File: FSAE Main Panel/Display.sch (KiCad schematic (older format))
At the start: 44 parts, among them U501 TLC6C598

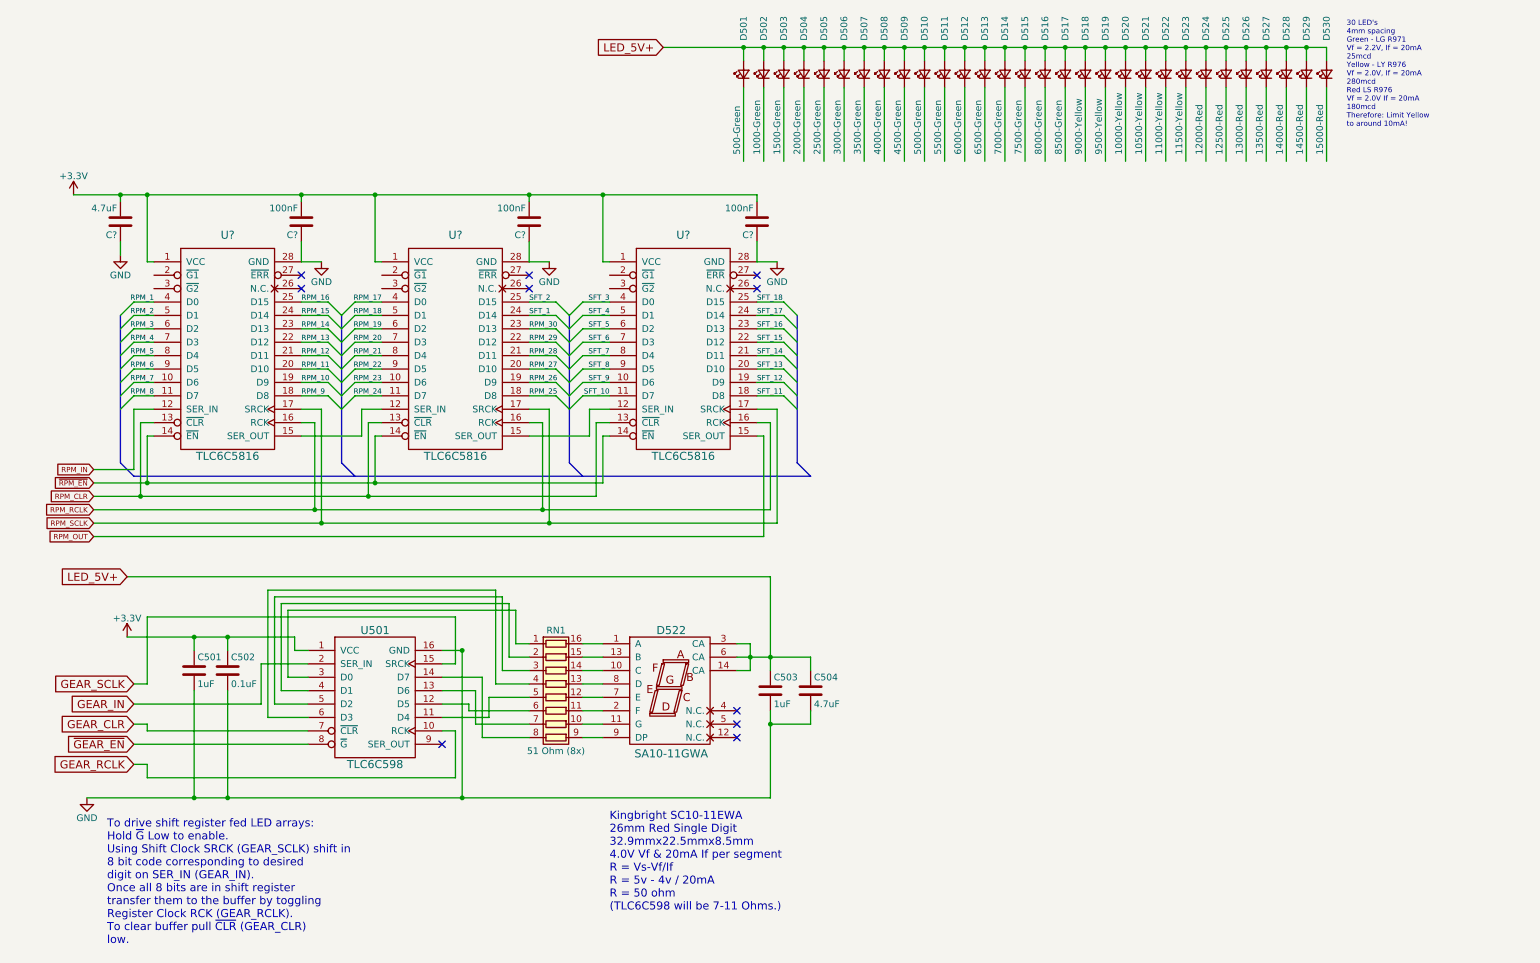
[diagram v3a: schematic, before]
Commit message: Added Blue shift LEDs and proper resistor arrays
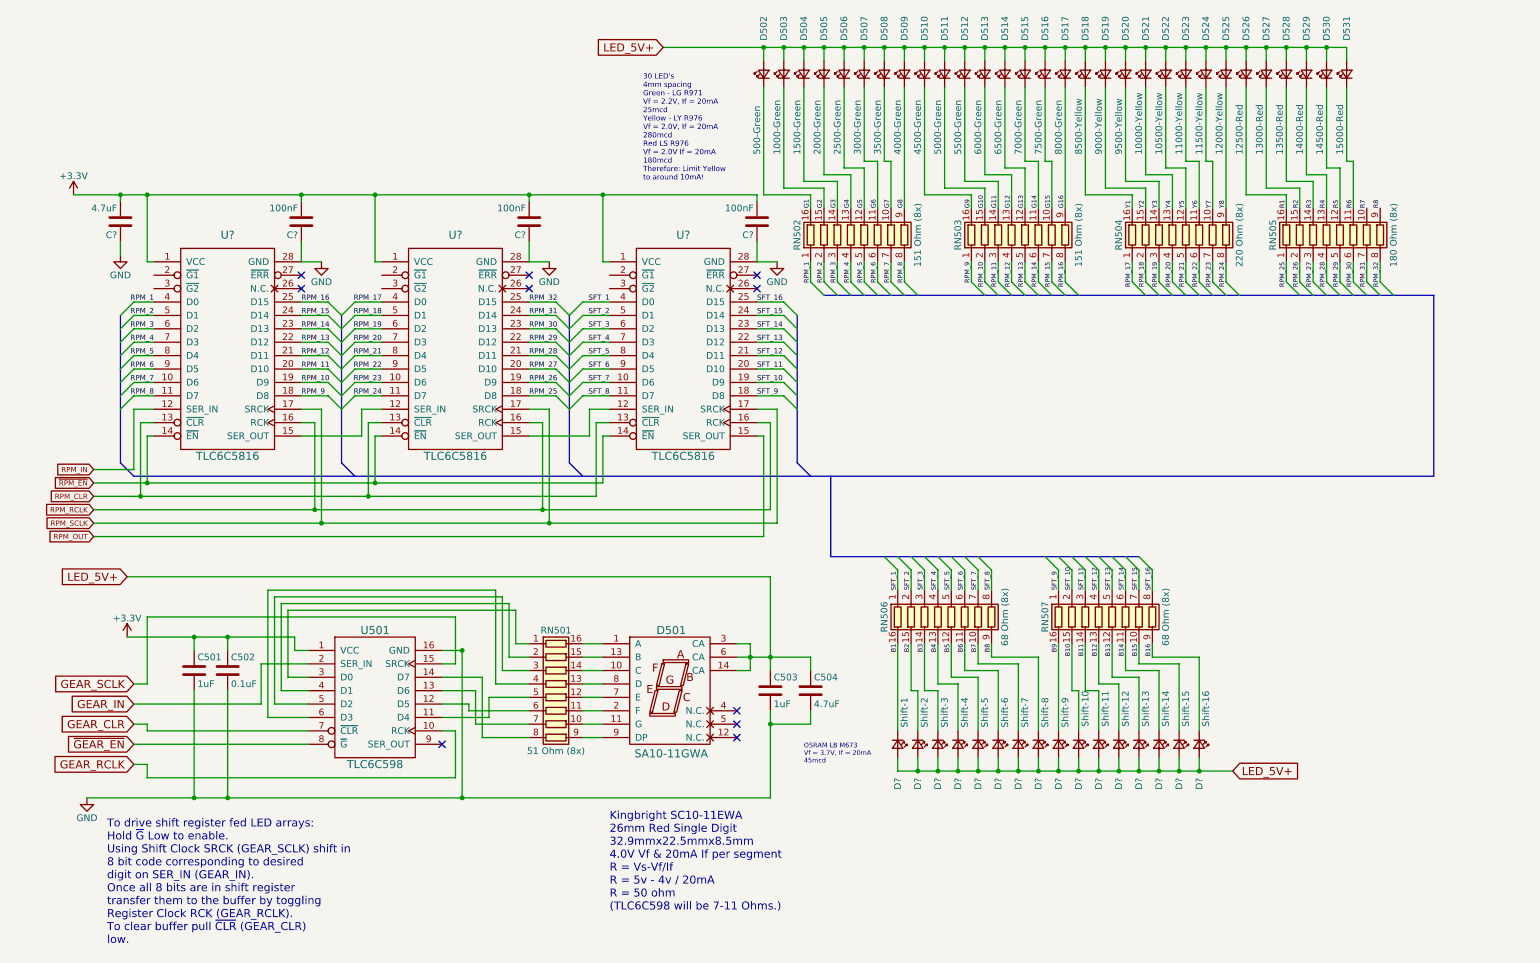
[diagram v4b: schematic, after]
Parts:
- removed D501: 500-Green, LEDs:LED_0805, symbol LED_Small
- added D531: 15000-Red, LEDs:LED_0805, symbol LED_Small
- added D?: Shift-1, LEDs:LED_0805, symbol LED_Small
- added D?: Shift-2, LEDs:LED_0805, symbol LED_Small
- added D?: Shift-3, LEDs:LED_0805, symbol LED_Small
- added D?: Shift-4, LEDs:LED_0805, symbol LED_Small
- added D?: Shift-5, LEDs:LED_0805, symbol LED_Small
- added D?: Shift-6, LEDs:LED_0805, symbol LED_Small
- added D?: Shift-7, LEDs:LED_0805, symbol LED_Small
- added D?: Shift-8, LEDs:LED_0805, symbol LED_Small
- added D?: Shift-9, LEDs:LED_0805, symbol LED_Small
- added D?: Shift-10, LEDs:LED_0805, symbol LED_Small
- added D?: Shift-11, LEDs:LED_0805, symbol LED_Small
- added D?: Shift-12, LEDs:LED_0805, symbol LED_Small
- added D?: Shift-13, LEDs:LED_0805, symbol LED_Small
- added D?: Shift-14, LEDs:LED_0805, symbol LED_Small
- added D?: Shift-15, LEDs:LED_0805, symbol LED_Small
- added D?: Shift-16, LEDs:LED_0805, symbol LED_Small
- added RN502, RN503: 151 Ohm (8x), Housings_SOIC:SOIC-16W_5.3x10.2mm_Pitch1.27mm, symbol R_Pack08
- added RN504: 220 Ohm (8x), Housings_SOIC:SOIC-16W_5.3x10.2mm_Pitch1.27mm, symbol R_Pack08
- added RN505: 180 Ohm (8x), Housings_SOIC:SOIC-16W_5.3x10.2mm_Pitch1.27mm, symbol R_Pack08
- added RN506, RN507: 68 Ohm (8x), Housings_SOIC:SOIC-16W_5.3x10.2mm_Pitch1.27mm, symbol R_Pack08
- D502: value 1000-Green -> 500-Green
- D503: value 1500-Green -> 1000-Green
- D504: value 2000-Green -> 1500-Green
- D505: value 2500-Green -> 2000-Green
- D506: value 3000-Green -> 2500-Green
- D507: value 3500-Green -> 3000-Green
- D508: value 4000-Green -> 3500-Green
- D509: value 4500-Green -> 4000-Green
- D510: value 5000-Green -> 4500-Green
- D511: value 5500-Green -> 5000-Green
- D512: value 6000-Green -> 5500-Green
- D513: value 6500-Green -> 6000-Green
- D514: value 7000-Green -> 6500-Green
- D515: value 7500-Green -> 7000-Green
- D516: value 8000-Green -> 7500-Green
- D517: value 8500-Green -> 8000-Green
- D518: value 9000-Yellow -> 8500-Yellow
- D519: value 9500-Yellow -> 9000-Yellow
- D520: value 10000-Yellow -> 9500-Yellow
- D521: value 10500-Yellow -> 10000-Yellow
- D522: value 11000-Yellow -> 10500-Yellow
- D523: value 11500-Yellow -> 11000-Yellow
- D524: value 12000-Red -> 11500-Yellow; Part Number LG R971 -> LY R976
- D525: value 12500-Red -> 12000-Yellow; Part Number LG R971 -> LY R976
- D526: value 13000-Red -> 12500-Red; Part Number LG R971 -> LS R976
- D527: value 13500-Red -> 13000-Red; Part Number LG R971 -> LS R976
- D528: value 14000-Red -> 13500-Red; Part Number LG R971 -> LS R976
- D529: value 14500-Red -> 14000-Red; Part Number LG R971 -> LS R976
- D530: value 15000-Red -> 14500-Red; Part Number LG R971 -> LS R976
- renumbered D522 to D501, RN1 to RN501
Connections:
- net labels added: B1, B10, B11, B12, B13, B14, B15, B16, B2, B3, B4, B5, B6, B7, B8, B9, G1, G10, G11, G12, G13, G14, G15, G16, G2, G3, G4, G5, G6, G7, G8, G9, R1, R2, R3, R4, R5, R6, R7, R8, RPM_31, RPM_32, Y1, Y2, Y3, Y4, Y5, Y6, Y7, Y8
- net labels removed: SFT_17, SFT_18
- wire segments 244 -> 407
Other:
- note added: "OSRAM LB M673\nVf = 3.7V, If = 20mA\n45mcd"

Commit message: Finished most LEDs, begun power regulators
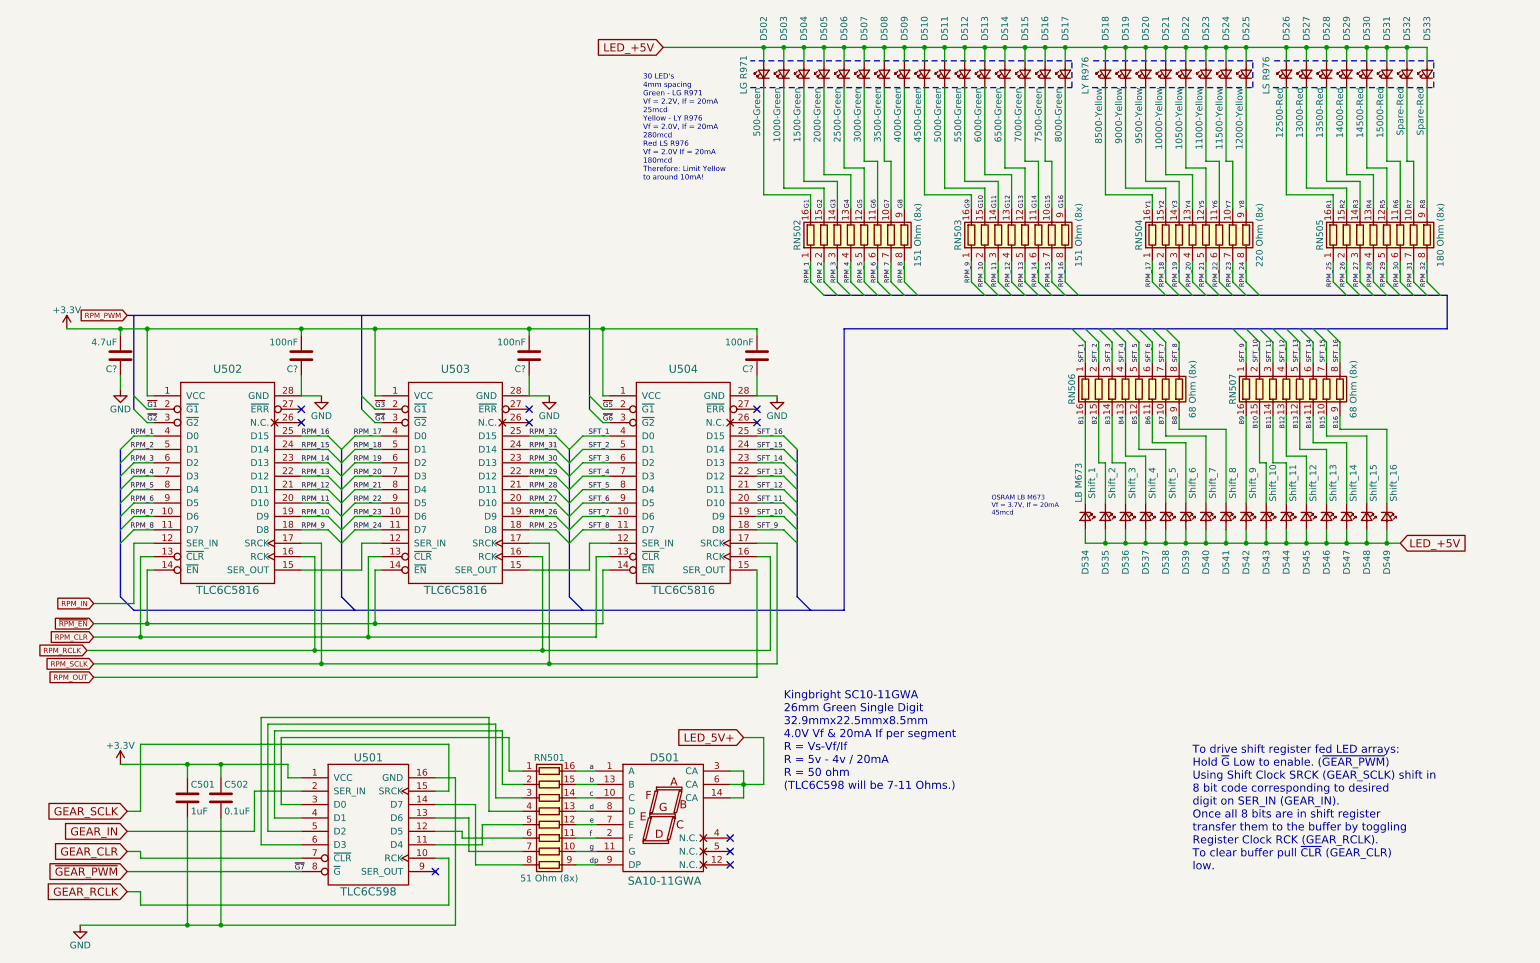
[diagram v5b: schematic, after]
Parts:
- removed C503: 1uF, symbol C
- removed C504: 4.7uF, symbol C
- removed D?: Shift-2, LEDs:LED_0805, symbol LED_Small
- removed D?: Shift-3, LEDs:LED_0805, symbol LED_Small
- removed D?: Shift-4, LEDs:LED_0805, symbol LED_Small
- removed D?: Shift-5, LEDs:LED_0805, symbol LED_Small
- removed D?: Shift-6, LEDs:LED_0805, symbol LED_Small
- removed D?: Shift-7, LEDs:LED_0805, symbol LED_Small
- removed D?: Shift-8, LEDs:LED_0805, symbol LED_Small
- removed D?: Shift-9, LEDs:LED_0805, symbol LED_Small
- removed D?: Shift-10, LEDs:LED_0805, symbol LED_Small
- removed D?: Shift-11, LEDs:LED_0805, symbol LED_Small
- removed D?: Shift-12, LEDs:LED_0805, symbol LED_Small
- removed D?: Shift-13, LEDs:LED_0805, symbol LED_Small
- removed D?: Shift-14, LEDs:LED_0805, symbol LED_Small
- removed D?: Shift-15, LEDs:LED_0805, symbol LED_Small
- removed D?: Shift-16, LEDs:LED_0805, symbol LED_Small
- added D532, D533: LS R976, LEDs:LED_0805, symbol LED_Small
- added D535, D536, D537, D538, D539, D540, D541, D542, D543, D544, D545, D546, D547, D548, D549: LB M673, LEDs:LED_0805, symbol LED_Small
- D502: value 500-Green -> LG R971; Function (none) -> 500-Green; Part Number LG R971 -> (none)
- D503: value 1000-Green -> LG R971; Function (none) -> 1000-Green; Part Number LG R971 -> (none)
- D504: value 1500-Green -> LG R971; Function (none) -> 1500-Green; Part Number LG R971 -> (none)
- D505: value 2000-Green -> LG R971; Function (none) -> 2000-Green; Part Number LG R971 -> (none)
- D506: value 2500-Green -> LG R971; Function (none) -> 2500-Green; Part Number LG R971 -> (none)
- D507: value 3000-Green -> LG R971; Function (none) -> 3000-Green; Part Number LG R971 -> (none)
- D508: value 3500-Green -> LG R971; Function (none) -> 3500-Green; Part Number LG R971 -> (none)
- D509: value 4000-Green -> LG R971; Function (none) -> 4000-Green; Part Number LG R971 -> (none)
- D510: value 4500-Green -> LG R971; Function (none) -> 4500-Green; Part Number LG R971 -> (none)
- D511: value 5000-Green -> LG R971; Function (none) -> 5000-Green; Part Number LG R971 -> (none)
- D512: value 5500-Green -> LG R971; Function (none) -> 5500-Green; Part Number LG R971 -> (none)
- D513: value 6000-Green -> LG R971; Function (none) -> 6000-Green; Part Number LG R971 -> (none)
- D514: value 6500-Green -> LG R971; Function (none) -> 6500-Green; Part Number LG R971 -> (none)
- D515: value 7000-Green -> LG R971; Function (none) -> 7000-Green; Part Number LG R971 -> (none)
- D516: value 7500-Green -> LG R971; Function (none) -> 7500-Green; Part Number LG R971 -> (none)
- D517: value 8000-Green -> LG R971; Function (none) -> 8000-Green; Part Number LG R971 -> (none)
- D518: value 8500-Yellow -> LY R976; Function (none) -> 8500-Yellow; Part Number LY R976 -> (none)
- D519: value 9000-Yellow -> LY R976; Function (none) -> 9000-Yellow; Part Number LY R976 -> (none)
- D520: value 9500-Yellow -> LY R976; Function (none) -> 9500-Yellow; Part Number LY R976 -> (none)
- D521: value 10000-Yellow -> LY R976; Function (none) -> 10000-Yellow; Part Number LY R976 -> (none)
- D522: value 10500-Yellow -> LY R976; Function (none) -> 10500-Yellow; Part Number LY R976 -> (none)
- D523: value 11000-Yellow -> LY R976; Function (none) -> 11000-Yellow; Part Number LY R976 -> (none)
- D524: value 11500-Yellow -> LY R976; Function (none) -> 11500-Yellow; Part Number LY R976 -> (none)
- D525: value 12000-Yellow -> LY R976; Function (none) -> 12000-Yellow; Part Number LY R976 -> (none)
- D526: value 12500-Red -> LS R976; Function (none) -> 12500-Red; Part Number LS R976 -> (none)
- D527: value 13000-Red -> LS R976; Function (none) -> 13000-Red; Part Number LS R976 -> (none)
- D528: value 13500-Red -> LS R976; Function (none) -> 13500-Red; Part Number LS R976 -> (none)
- D529: value 14000-Red -> LS R976; Function (none) -> 14000-Red; Part Number LS R976 -> (none)
- D530: value 14500-Red -> LS R976; Function (none) -> 14500-Red; Part Number LS R976 -> (none)
- D531: value 15000-Red -> LS R976; Function (none) -> 15000-Red; Part Number LS R976 -> (none)
- D534: renamed from D?; value Shift-1 -> LB M673; Function (none) -> Shift_1; Part Number LB M673 -> (none)
- gave numbers to parts that had none: 3
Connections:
- net B10: now also D543.1 (K)
- net B11: now also D544.1 (K)
- net B12: now also D545.1 (K)
- net B13: now also D546.1 (K)
- net B14: now also D547.1 (K)
- net B15: now also D548.1 (K)
- net B16: now also D549.1 (K)
- net B2: now also D535.1 (K)
- net B3: now also D536.1 (K)
- net B4: now also D537.1 (K)
- net B5: now also D538.1 (K)
- net B6: now also D539.1 (K)
- net B7: now also D540.1 (K)
- net B8: now also D541.1 (K)
- net B9: now also D542.1 (K)
- net LED_5V+: no longer D502.2 (A), D503.2 (A), D504.2 (A), D505.2 (A), D506.2 (A), D507.2 (A), D508.2 (A), D509.2 (A), D510.2 (A), D511.2 (A), D512.2 (A), D513.2 (A), D514.2 (A), D515.2 (A), D516.2 (A), D517.2 (A), D518.2 (A), D519.2 (A), D520.2 (A), D521.2 (A), D522.2 (A), D523.2 (A), D524.2 (A), D525.2 (A), D526.2 (A), D527.2 (A), D528.2 (A), D529.2 (A), D530.2 (A), D531.2 (A), D534.2 (A)
- net R7: now also D532.1 (K)
- net R8: now also D533.1 (K)
- net g: now reaches D501.11 (G), RN501.10 (R7.2)
- net f: now reaches D501.2 (F), RN501.11 (R6.2)
- net e: now reaches D501.7 (E), RN501.12 (R5.2)
- net d: now reaches D501.8 (D), RN501.13 (R4.2)
- net c: now reaches D501.10 (C), RN501.14 (R3.2)
- net b: now reaches D501.13 (B), RN501.15 (R2.2)
- net a: now reaches D501.1 (A), RN501.16 (R1.2)
- net dp: now reaches D501.9 (DP), RN501.9 (R8.2)
- net ~G1: now reaches U502.2 (~G1)
- net ~G2: now reaches U502.3 (~G2)
- net ~G3: now reaches U503.2 (~G1)
- net ~G4: now reaches U503.3 (~G2)
- net ~G5: now reaches U504.2 (~G1)
- net ~G6: now reaches U504.3 (~G2)
- net ~GEAR_EN renamed ~GEAR_PWM
- new net LED_+5V: D502.2 (A), D503.2 (A), D504.2 (A), D505.2 (A), D506.2 (A), D507.2 (A), D508.2 (A), D509.2 (A), D510.2 (A), D511.2 (A), D512.2 (A), D513.2 (A), D514.2 (A), D515.2 (A), D516.2 (A), D517.2 (A), D518.2 (A), D519.2 (A), D520.2 (A), D521.2 (A), D522.2 (A), D523.2 (A), D524.2 (A), D525.2 (A), D526.2 (A), D527.2 (A), D528.2 (A), D529.2 (A), D530.2 (A), D531.2 (A), D532.2 (A), D533.2 (A), D534.2 (A), D535.2 (A), D536.2 (A), D537.2 (A), D538.2 (A), D539.2 (A), D540.2 (A), D541.2 (A), D542.2 (A), D543.2 (A), D544.2 (A), D545.2 (A), D546.2 (A), D547.2 (A), D548.2 (A), D549.2 (A)
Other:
- note added: "Kingbright SC10-11GWA\n26mm Green Single Digit\n32.9mmx22.5mmx8.5mm\n4.0V Vf & 20mA If per segment\nR = Vs-Vf/If\nR = 5v - 4v / 20mA\nR = 50 ohm\n(TLC6C598 will be 7-11 Ohms.)"
- note added: "To drive shift register fed LED arrays:\nHold ~G~ Low to enable. (~GEAR_PWM~)\nUsing Shift Clock SRCK (GEAR_SCLK) shift in\n8 bit code corresponding to desired\ndigit on SER_IN (GEAR_IN).\nOnce all 8 bits are in shift register\ntransfer them to the buffer by toggling\nRegister Clock RCK (GEAR_RCLK).\nTo clear buffer pull ~CLR~ (GEAR_CLR)\nlow."
- note removed: "Kingbright SC10-11EWA\n26mm Red Single Digit\n32.9mmx22.5mmx8.5mm\n4.0V Vf & 20mA If per segment\nR = Vs-Vf/If\nR = 5v - 4v / 20mA\nR = 50 ohm\n(TLC6C598 will be 7-11 Ohms.)"
- note removed: "To drive shift register fed LED arrays:\nHold ~G~ Low to enable.\nUsing Shift Clock SRCK (GEAR_SCLK) shift in\n8 bit code corresponding to desired\ndigit on SER_IN (GEAR_IN).\nOnce all 8 bits are in shift register\ntransfer them to the buffer by toggling\nRegister Clock RCK (GEAR_RCLK).\nTo clear buffer pull ~CLR~ (GEAR_CLR)\nlow."
- moved on the sheet: C501, C502, C?, D501, D518, D526, D534, RN501, RN504, RN505, RN506, RN507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

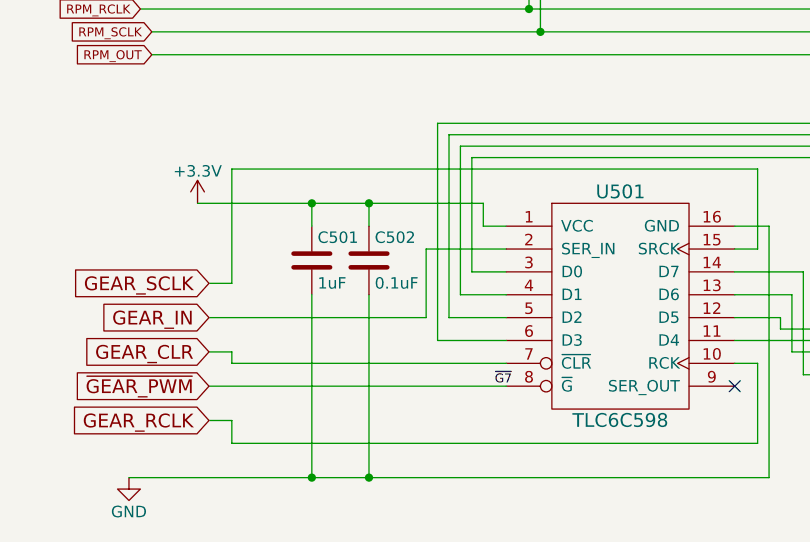
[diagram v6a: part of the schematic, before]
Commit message: Cortex debugger, GPIO pinning, minor fixes
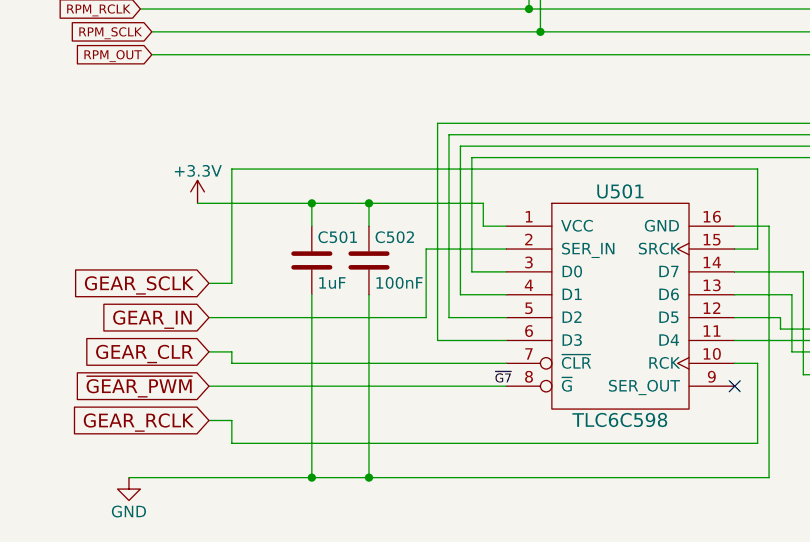
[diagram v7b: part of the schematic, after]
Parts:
- C502: value 0.1uF -> 100nF
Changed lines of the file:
@@
 LIBS:samd21g18a-au
 LIBS:zldo1117-5v
+LIBS:cortex_debug
 LIBS:FSAE Main Panel-cache
 EELAYER 25 0
@@
 P 1950 6500
 F 0 "C502" H 1975 6600 50  0000 L CNN
-F 1 "0.1uF" H 1975 6400 50  0000 L CNN
+F 1 "100nF" H 1975 6400 50  0000 L CNN
 F 2 "" H 1988 6350 50  0001 C CNN
 F 3 "" H 1950 6500 50  0001 C CNN
